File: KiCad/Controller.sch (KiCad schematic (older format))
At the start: 9 parts, among them IC4 ATMEGA8-P, SW1 Reverse, SW2 Start, SW3 Lights, U5 Linkura

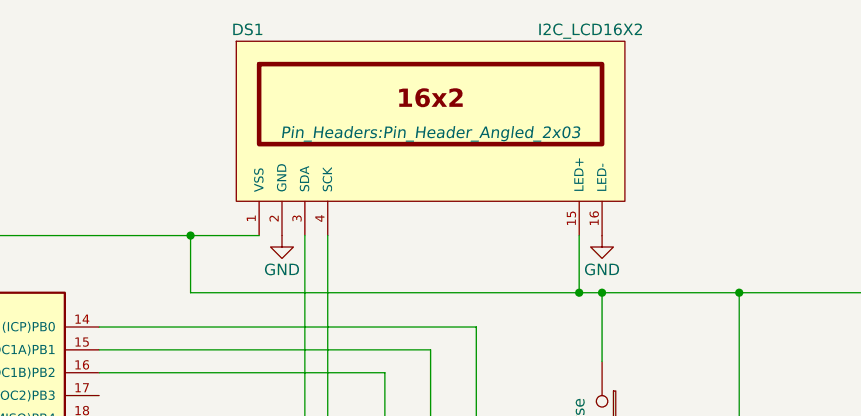
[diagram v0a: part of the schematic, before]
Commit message: Updated the schematics and started with the PCB
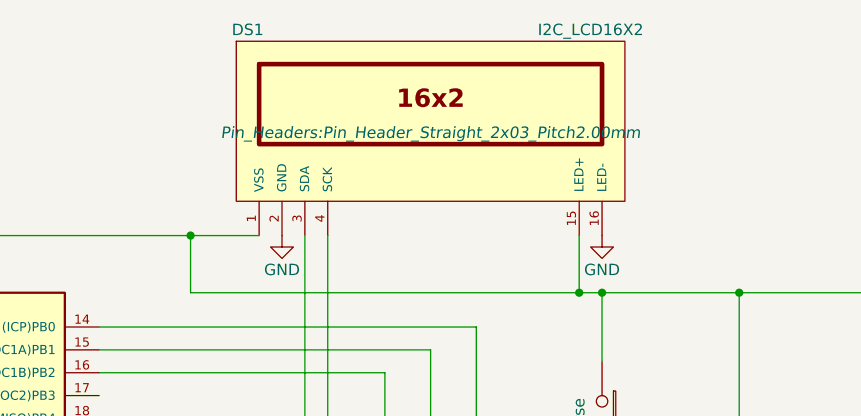
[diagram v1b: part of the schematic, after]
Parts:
- DS1: footprint Pin_Headers:Pin_Header_Angled_2x03 -> Pin_Headers:Pin_Header_Straight_2x03_Pitch2.00mm
- R34, R35, R36: footprint Resistors_ThroughHole:Resistor_Horizontal_RM20mm -> Resistors_ThroughHole:Resistor_Vertical_RM5mm
- SW1, SW2, SW3, U5: footprint Wire_Pads:SolderWirePad_2x_0-8mmDrill -> Wire_Connections_Bridges:WireConnection_1.50mmDrill
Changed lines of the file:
@@
 $Descr A4 11693 8268
 encoding utf-8
-Sheet 6 7
+Sheet 5 6
 Title ""
 Date ""
@@
 F 0 "U5" H 4300 6750 60  0000 C CNN
 F 1 "Linkura" H 3800 6650 60  0000 C CNN
-F 2 "Wire_Pads:SolderWirePad_2x_0-8mmDrill" H 4000 6600 60  0001 C CNN
+F 2 "Wire_Connections_Bridges:WireConnection_1.50mmDrill" H 4000 6600 60  0001 C CNN
 F 3 "" H 4000 6600 60  0000 C CNN
 	1    4000 6600
@@
 F 0 "DS1" H 4200 3050 50  0000 C CNN
 F 1 "I2C_LCD16X2" H 5700 3050 50  0000 C CNN
-F 2 "Pin_Headers:Pin_Header_Angled_2x03" H 5000 2600 50  0000 C CIN
+F 2 "Pin_Headers:Pin_Header_Straight_2x03_Pitch2.00mm" H 5000 2600 50  0000 C CIN
 F 3 "" H 5000 2650 50  0000 C CNN
 	1    5000 2650
@@
 F 0 "SW1" H 5900 4110 50  0000 C CNN
 F 1 "Reverse" H 5750 3900 50  0000 C CNN
-F 2 "Wire_Pads:SolderWirePad_2x_0-8mmDrill" H 5750 4000 50  0001 C CNN
+F 2 "Wire_Connections_Bridges:WireConnection_1.50mmDrill" H 5750 4000 50  0001 C CNN
 F 3 "" H 5750 4000 50  0000 C CNN
 	1    5750 4000
@@
 F 0 "SW2" H 6500 4410 50  0000 C CNN
 F 1 "Start" H 6350 4220 50  0000 C CNN
-F 2 "Wire_Pads:SolderWirePad_2x_0-8mmDrill" H 6350 4300 50  0001 C CNN
+F 2 "Wire_Connections_Bridges:WireConnection_1.50mmDrill" H 6350 4300 50  0001 C CNN
 F 3 "" H 6350 4300 50  0000 C CNN
 	1    6350 4300
@@
 F 0 "SW3" H 7100 4710 50  0000 C CNN
 F 1 "Lights" H 6950 4520 50  0000 C CNN
-F 2 "Wire_Pads:SolderWirePad_2x_0-8mmDrill" H 6950 4600 50  0001 C CNN
+F 2 "Wire_Connections_Bridges:WireConnection_1.50mmDrill" H 6950 4600 50  0001 C CNN
 F 3 "" H 6950 4600 50  0000 C CNN
 	1    6950 4600
@@
 F 0 "R34" V 5680 4450 50  0000 C CNN
 F 1 "R" V 5600 4450 50  0000 C CNN
-F 2 "Resistors_ThroughHole:Resistor_Horizontal_RM20mm" V 5530 4450 50  0001 C CNN
+F 2 "Resistors_ThroughHole:Resistor_Vertical_RM5mm" V 5530 4450 50  0001 C CNN
 F 3 "" H 5600 4450 50  0000 C CNN
 	1    5600 4450
@@
 F 0 "R35" V 6280 4750 50  0000 C CNN
 F 1 "R" V 6200 4750 50  0000 C CNN
-F 2 "Resistors_ThroughHole:Resistor_Horizontal_RM20mm" V 6130 4750 50  0001 C CNN
+F 2 "Resistors_ThroughHole:Resistor_Vertical_RM5mm" V 6130 4750 50  0001 C CNN
 F 3 "" H 6200 4750 50  0000 C CNN
 	1    6200 4750
@@
 F 0 "R36" V 6880 5050 50  0000 C CNN
 F 1 "R" V 6800 5050 50  0000 C CNN
-F 2 "Resistors_ThroughHole:Resistor_Horizontal_RM20mm" V 6730 5050 50  0001 C CNN
+F 2 "Resistors_ThroughHole:Resistor_Vertical_RM5mm" V 6730 5050 50  0001 C CNN
 F 3 "" H 6800 5050 50  0000 C CNN
 	1    6800 5050
